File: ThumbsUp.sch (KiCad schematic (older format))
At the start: 150 parts, among them IC1 RP2040, IC2 W25Q128JVSIM, J1 Conn_01x04_Male, J10 Raiser_Male, J11 Raiser_Female, J12 Raiser_Male, J13 Raiser_Female, J14 Raiser_Male, J15 Raiser_Female, J16 Raiser_Male, J17 Raiser_Female, J18 Raiser_Male, J19 52559-1233, J2 Conn_01x04_Male, J20 Conn_01x04_Female, J21 Conn_01x04_Female, J22 Conn_01x04_Female, J23 Conn_01x04_Female, J24 Conn_01x04_Male, J25 Conn_01x04_Male, J26 Conn_01x04_Male, J27 Conn_01x04_Male, J28 Conn_01x04_Female, J29 Conn_01x04_Female, J3 Conn_01x04_Female, J30 Conn_01x04_Female, J31 Conn_01x04_Female, J4 Conn_01x04_Male, J5 Conn_01x04_Female, J6 Conn_01x04_Male, J7 Conn_01x04_Male, J8 Conn_01x04_Male, J9 Raiser_Female, U1 NCP1117-3.3_SOT223, Y1 ABLS-12.000MHZ-B4-T

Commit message: Wiring continued
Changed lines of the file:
@@
 Wire Wire Line
 	12550 2900 12200 2900
-$Comp
-L RP2040:RP2040 IC1
-U 1 1 6393717F
-P 2050 2550
-F 0 "IC1" H 4094 1996 50  0000 L CNN
-F 1 "RP2040" H 4094 1905 50  0000 L CNN
-F 2 "RP2040:QFN40P700X700X90-57N-D" H 3900 3250 50  0001 L CNN
-F 3 "https://datasheets.raspberrypi.org/rp2040/rp2040-datasheet.pdf" H 3900 3150 50  0001 L CNN
-F 4 "Microcontroller in QFN Package" H 3900 3050 50  0001 L CNN "Description"
-F 5 "0.9" H 3900 2950 50  0001 L CNN "Height"
-F 6 "RASPBERRY-PI" H 3900 2850 50  0001 L CNN "Manufacturer_Name"
-F 7 "RP2040" H 3900 2750 50  0001 L CNN "Manufacturer_Part_Number"
-F 8 "" H 3900 2650 50  0001 L CNN "Mouser Part Number"
-F 9 "" H 3900 2550 50  0001 L CNN "Mouser Price/Stock"
-F 10 "" H 3900 2450 50  0001 L CNN "Arrow Part Number"
-F 11 "" H 3900 2350 50  0001 L CNN "Arrow Price/Stock"
-F 12 "" H 3900 2250 50  0001 L CNN "Mouser Testing Part Number"
-F 13 "" H 3900 2150 50  0001 L CNN "Mouser Testing Price/Stock"
-	1    2050 2550
-	1    0    0    -1
-$EndComp
 Wire Wire Line
 	2050 3450 1550 3450
@@
 Wire Wire Line
 	3050 5100 1550 5100
-Wire Wire Line
-	1550 5100 1550 3450
 Connection ~ 1550 3450
 Wire Wire Line
@@
 Wire Wire Line
 	1550 1200 1550 2550
-Wire Wire Line
-	2050 2550 1550 2550
 Connection ~ 1550 2550
 Wire Wire Line
@@
 	3550 5050 3550 5350
 Connection ~ 3550 5350
+Wire Wire Line
+	1550 5100 1550 3450
+Wire Wire Line
+	2050 2550 1550 2550
+$Comp
+L RP2040:RP2040 IC1
+U 1 1 6393717F
+P 2050 2550
+F 0 "IC1" H 4094 1996 50  0000 L CNN
+F 1 "RP2040" H 4094 1905 50  0000 L CNN
+F 2 "RP2040:QFN40P700X700X90-57N-D" H 3900 3250 50  0001 L CNN
+F 3 "https://datasheets.raspberrypi.org/rp2040/rp2040-datasheet.pdf" H 3900 3150 50  0001 L CNN
+F 4 "Microcontroller in QFN Package" H 3900 3050 50  0001 L CNN "Description"
+F 5 "0.9" H 3900 2950 50  0001 L CNN "Height"
+F 6 "RASPBERRY-PI" H 3900 2850 50  0001 L CNN "Manufacturer_Name"
+F 7 "RP2040" H 3900 2750 50  0001 L CNN "Manufacturer_Part_Number"
+F 8 "" H 3900 2650 50  0001 L CNN "Mouser Part Number"
+F 9 "" H 3900 2550 50  0001 L CNN "Mouser Price/Stock"
+F 10 "" H 3900 2450 50  0001 L CNN "Arrow Part Number"
+F 11 "" H 3900 2350 50  0001 L CNN "Arrow Price/Stock"
+F 12 "" H 3900 2250 50  0001 L CNN "Mouser Testing Part Number"
+F 13 "" H 3900 2150 50  0001 L CNN "Mouser Testing Price/Stock"
+	1    2050 2550
+	1    0    0    -1
+$EndComp
+Text GLabel 4050 2650 2    50   Input ~ 0
+ROW2
+Text GLabel 4050 2750 2    50   Input ~ 0
+ROW3
+Text GLabel 4050 2850 2    50   Input ~ 0
+COL5
+Text GLabel 4050 2950 2    50   Input ~ 0
+COL3
+Text GLabel 4050 3050 2    50   Input ~ 0
+COL2
+Text GLabel 4050 3150 2    50   Input ~ 0
+COL1
+Text GLabel 4050 3250 2    50   Input ~ 0
+COL0
+Text GLabel 4050 3350 2    50   Input ~ 0
+COL4
+Text GLabel 2050 2650 0    50   Input ~ 0
+ROW0
+Text GLabel 2050 2750 0    50   Input ~ 0
+ROW1
+Text GLabel 2050 2850 0    50   Input ~ 0
+COL7
+Text GLabel 2050 2950 0    50   Input ~ 0
+COL6
+Text GLabel 2050 3050 0    50   Input ~ 0
+COL8
+Text GLabel 2050 3150 0    50   Input ~ 0
+COL9
+Text GLabel 2050 3250 0    50   Input ~ 0
+COLA
+Text GLabel 2050 3350 0    50   Input ~ 0
+COLB
 $EndSCHEMATC

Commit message: Replaced the mini-USB connector with USB-C
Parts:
- removed USB1: Molex-0548190589, random-keyboard-parts:Molex-0548190589, symbol ThumbsUp-rescue:Molex-0548190589-random-keyboard-parts
- added J32: USB_C_Receptacle_USB2.0, Connector_USB:USB_C_Receptacle_Palconn_UTC16-G, symbol Connector:USB_C_Receptacle_USB2.0
- added R8, R9: 5.1k, Resistor_SMD:R_0805_2012Metric, symbol Device:R_Small
- BOOTSEL1, RUN1: footprint TL1016AAF220QG -> TL1016AAF220QG:TL1016AAF220QG
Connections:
- wire segments 474 -> 481
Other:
- moved on the sheet: BOOTSEL1, C1, C10, C12, C13, C14, C15, C16, C17, C2, C3, C4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

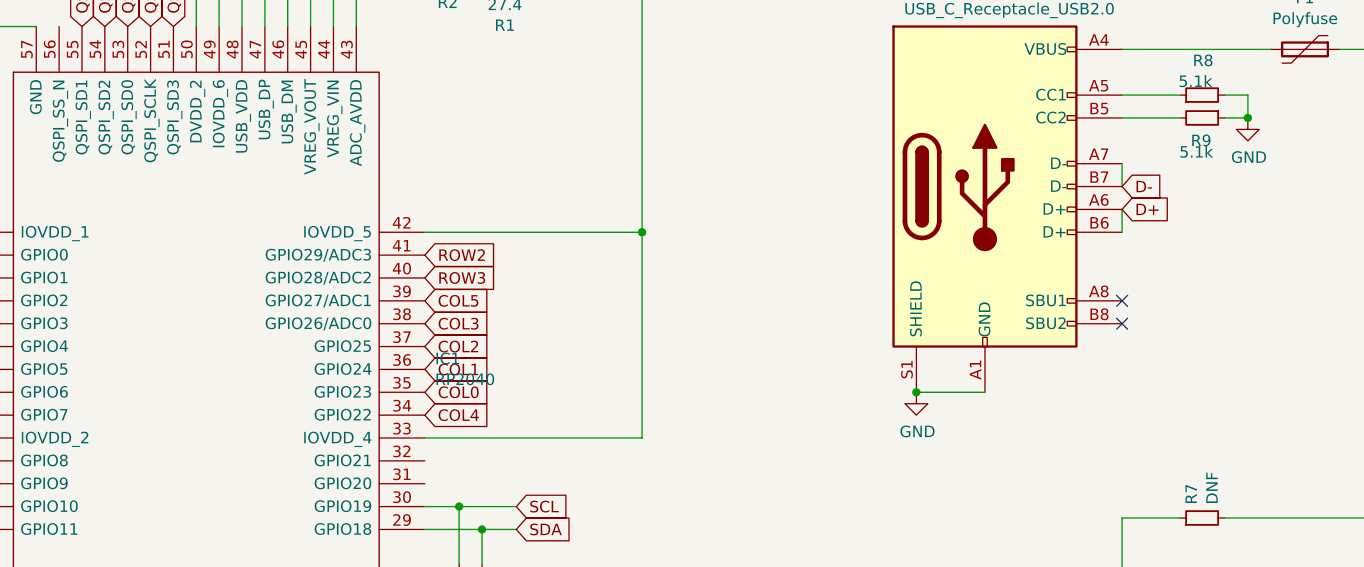
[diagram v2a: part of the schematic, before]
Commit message: Some schema elements rearranged
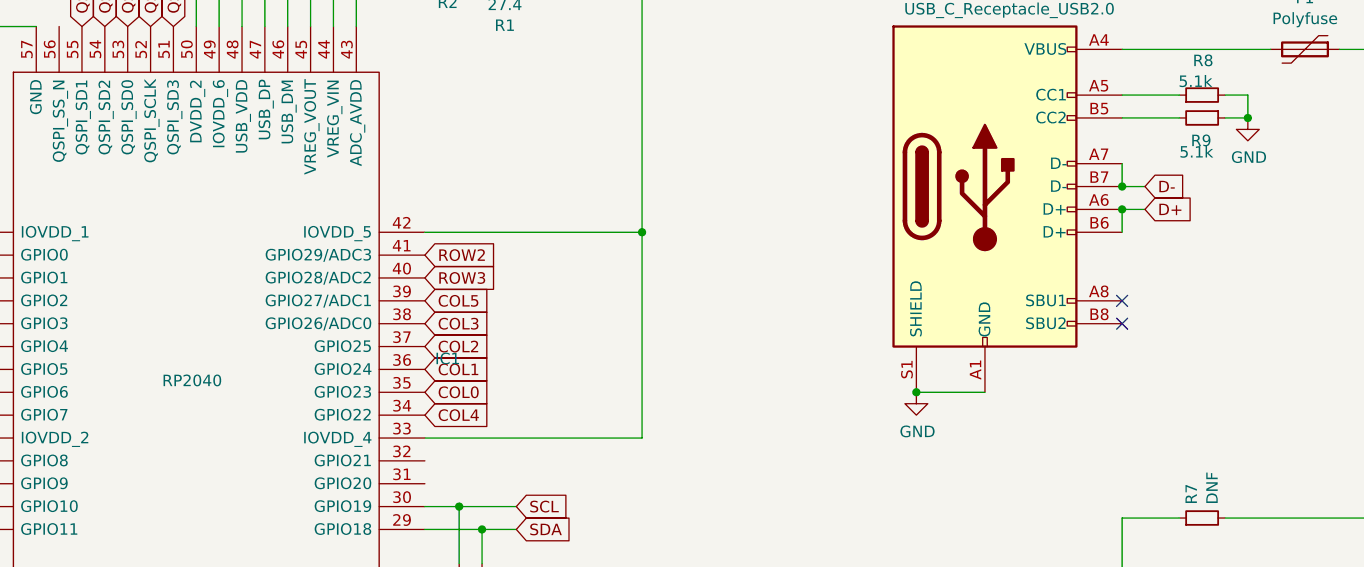
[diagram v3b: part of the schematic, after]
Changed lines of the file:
@@
 Wire Wire Line
 	8350 1600 8350 1750
-Text GLabel 7100 2350 2    50   Input ~ 0
+Text GLabel 7200 2350 2    50   Input ~ 0
 D-
-Text GLabel 7100 2450 2    50   Input ~ 0
+Text GLabel 7200 2450 2    50   Input ~ 0
 D+
 $Comp
@@
 P 2050 2550
 F 0 "IC1" H 4094 1996 50  0000 L CNN
-F 1 "RP2040" H 4094 1905 50  0000 L CNN
+F 1 "RP2040" H 2900 1900 50  0000 L CNN
 F 2 "RP2040:QFN40P700X700X90-57N-D" H 3900 3250 50  0001 L CNN
 F 3 "https://datasheets.raspberrypi.org/rp2040/rp2040-datasheet.pdf" H 3900 3150 50  0001 L CNN
@@
 NoConn ~ 7100 2850
 NoConn ~ 7100 2950
+Wire Wire Line
+	7100 2350 7200 2350
+Connection ~ 7100 2350
+Wire Wire Line
+	7100 2450 7200 2450
+Connection ~ 7100 2450
 $EndSCHEMATC

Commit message: Restored the schematics file which was overridden by mistake
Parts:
- added J33: STX-3501-3N, STX-3501-3N:STX35013N, symbol STX-3501-3N:STX-3501-3N
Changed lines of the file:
@@
 	7100 2450 7200 2450
 Connection ~ 7100 2450
+$Comp
+L STX-3501-3N:STX-3501-3N J33
+U 1 1 63B2DFF1
+P 8200 2800
+F 0 "J33" H 8600 3065 50  0000 C CNN
+F 1 "STX-3501-3N" H 8600 2974 50  0000 C CNN
+F 2 "STX-3501-3N:STX35013N" H 8850 2900 50  0001 L CNN
+F 3 "https://datasheet.datasheetarchive.com/originals/distributors/Datasheets_SAMA/ae9d1df0991347f2f81145ba35ca04dc.pdf" H 8850 2800 50  0001 L CNN
+F 4 "Phone Connectors 3.5mm S LUGS STEREO 3P THRU HOLE" H 8850 2700 50  0001 L CNN "Description"
+F 5 "5" H 8850 2600 50  0001 L CNN "Height"
+F 6 "Kycon" H 8850 2500 50  0001 L CNN "Manufacturer_Name"
+F 7 "STX-3501-3N" H 8850 2400 50  0001 L CNN "Manufacturer_Part_Number"
+F 8 "806-STX-3501-3N" H 8850 2300 50  0001 L CNN "Mouser Part Number"
+F 9 "https://www.mouser.co.uk/ProductDetail/Kycon/STX-3501-3N?qs=BBNwCsfFaznpJt4o1Jp%2FTg%3D%3D" H 8850 2200 50  0001 L CNN "Mouser Price/Stock"
+F 10 "" H 8850 2100 50  0001 L CNN "Arrow Part Number"
+F 11 "" H 8850 2000 50  0001 L CNN "Arrow Price/Stock"
+F 12 "" H 8850 1900 50  0001 L CNN "Mouser Testing Part Number"
+F 13 "" H 8850 1800 50  0001 L CNN "Mouser Testing Price/Stock"
+	1    8200 2800
+	1    0    0    -1
+$EndComp
 $EndSCHEMATC

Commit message: Added a missing line SS-N
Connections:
- net labels added: QSPI_SSN
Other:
- moved on the sheet: BOOTSEL1, R3
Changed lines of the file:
@@
 L Device:R_Small R3
 U 1 1 616D4E45
-P 7000 4350
-F 0 "R3" H 7059 4396 50  0000 L CNN
-F 1 "10k" H 7059 4305 50  0000 L CNN
-F 2 "Resistor_SMD:R_0805_2012Metric" H 7000 4350 50  0001 C CNN
-F 3 "~" H 7000 4350 50  0001 C CNN
-	1    7000 4350
+P 7000 3800
+F 0 "R3" H 7059 3846 50  0000 L CNN
+F 1 "10k" H 7059 3755 50  0000 L CNN
+F 2 "Resistor_SMD:R_0805_2012Metric" H 7000 3800 50  0001 C CNN
+F 3 "~" H 7000 3800 50  0001 C CNN
+	1    7000 3800
 	0    -1   -1   0
 $EndComp
@@
 	3350 1350 3350 1650
 $Comp
-L W25Q128JVSIM:W25Q128JVSIM IC2
-U 1 1 64048C65
-P 7100 4350
-F 0 "IC2" H 8200 4615 50  0000 C CNN
-F 1 "W25Q128JVSIM" H 8200 4524 50  0000 C CNN
-F 2 "W25Q128JVSIM:SOIC127P790X216-8N" H 9150 4450 50  0001 L CNN
-F 3 "https://www.winbond.com/hq/search-resource-file.jsp?partNo=W25Q128JVSIM&type=datasheet" H 9150 4350 50  0001 L CNN
-F 4 "128M-bit Serial Flash Memory with uniform 4KB sectors and Dual/Quad SPI" H 9150 4250 50  0001 L CNN "Description"
-F 5 "2.16" H 9150 4150 50  0001 L CNN "Height"
-F 6 "Winbond" H 9150 4050 50  0001 L CNN "Manufacturer_Name"
-F 7 "W25Q128JVSIM" H 9150 3950 50  0001 L CNN "Manufacturer_Part_Number"
-F 8 "454-W25Q128JVSIM" H 9150 3850 50  0001 L CNN "Mouser Part Number"
-F 9 "https://www.mouser.co.uk/ProductDetail/Winbond/W25Q128JVSIM?qs=qSfuJ%252Bfl%2Fd6d7A5WLggp6w%3D%3D" H 9150 3750 50  0001 L CNN "Mouser Price/Stock"
-F 10 "W25Q128JVSIM" H 9150 3650 50  0001 L CNN "Arrow Part Number"
-F 11 "https://www.arrow.com/en/products/w25q128jvsim/winbond-electronics?region=nac" H 9150 3550 50  0001 L CNN "Arrow Price/Stock"
-F 12 "" H 9150 3450 50  0001 L CNN "Mouser Testing Part Number"
-F 13 "" H 9150 3350 50  0001 L CNN "Mouser Testing Price/Stock"
-	1    7100 4350
-	1    0    0    -1
-$EndComp
-$Comp
 L Device:C_Small C10
 U 1 1 6404A526
@@
 L TL1016AAF220QG:TL1016AAF220QG BOOTSEL1
 U 1 1 63B7CD0C
-P 6250 4350
-F 0 "BOOTSEL1" V 6100 4100 50  0000 L CNN
-F 1 "TL1016AAF220QG" V 6200 4000 50  0000 L CNN
-F 2 "TL1016AAF220QG:TL1016AAF220QG" H 6900 4450 50  0001 L CNN
-F 3 "https://eu.mouser.com/datasheet/2/140/E_Switch_05112022_TL1016_Datasheet-2943618.pdf" H 6900 4350 50  0001 L CNN
-F 4 "Tactile Switches Tactile Switch SPST OFF-(ON) 50mA 12VDC" H 6900 4250 50  0001 L CNN "Description"
-F 5 "1.35" H 6900 4150 50  0001 L CNN "Height"
-F 6 "E-Switch" H 6900 4050 50  0001 L CNN "Manufacturer_Name"
-F 7 "TL1016AAF220QG" H 6900 3950 50  0001 L CNN "Manufacturer_Part_Number"
-F 8 "612-TL1016AAF220QG" H 6900 3850 50  0001 L CNN "Mouser Part Number"
-F 9 "https://www.mouser.co.uk/ProductDetail/E-Switch/TL1016AAF220QG?qs=t7xnP681wgW5zrSpkWH91Q%3D%3D" H 6900 3750 50  0001 L CNN "Mouser Price/Stock"
-F 10 "" H 6900 3650 50  0001 L CNN "Arrow Part Number"
-F 11 "" H 6900 3550 50  0001 L CNN "Arrow Price/Stock"
-F 12 "" H 6900 3450 50  0001 L CNN "Mouser Testing Part Number"
-F 13 "" H 6900 3350 50  0001 L CNN "Mouser Testing Price/Stock"
-	1    6250 4350
+P 6250 3800
+F 0 "BOOTSEL1" V 6100 3550 50  0000 L CNN
+F 1 "TL1016AAF220QG" V 6200 3450 50  0000 L CNN
+F 2 "TL1016AAF220QG:TL1016AAF220QG" H 6900 3900 50  0001 L CNN
+F 3 "https://eu.mouser.com/datasheet/2/140/E_Switch_05112022_TL1016_Datasheet-2943618.pdf" H 6900 3800 50  0001 L CNN
+F 4 "Tactile Switches Tactile Switch SPST OFF-(ON) 50mA 12VDC" H 6900 3700 50  0001 L CNN "Description"
+F 5 "1.35" H 6900 3600 50  0001 L CNN "Height"
+F 6 "E-Switch" H 6900 3500 50  0001 L CNN "Manufacturer_Name"
+F 7 "TL1016AAF220QG" H 6900 3400 50  0001 L CNN "Manufacturer_Part_Number"
+F 8 "612-TL1016AAF220QG" H 6900 3300 50  0001 L CNN "Mouser Part Number"
+F 9 "https://www.mouser.co.uk/ProductDetail/E-Switch/TL1016AAF220QG?qs=t7xnP681wgW5zrSpkWH91Q%3D%3D" H 6900 3200 50  0001 L CNN "Mouser Price/Stock"
+F 10 "" H 6900 3100 50  0001 L CNN "Arrow Part Number"
+F 11 "" H 6900 3000 50  0001 L CNN "Arrow Price/Stock"
+F 12 "" H 6900 2900 50  0001 L CNN "Mouser Testing Part Number"
+F 13 "" H 6900 2800 50  0001 L CNN "Mouser Testing Price/Stock"
+	1    6250 3800
 	0    1    1    0
 $EndComp
 Wire Wire Line
-	6250 4350 6450 4350
-Wire Wire Line
-	6250 5150 6450 5150
+	6250 3800 6450 3800
 Wire Wire Line
-	6450 5150 6450 4350
-Connection ~ 6450 4350
+	6250 4600 6450 4600
 Wire Wire Line
-	6450 4350 6900 4350
+	6450 4600 6450 3800
+Connection ~ 6450 3800
 Wire Wire Line
-	6150 4350 5950 4350
+	6150 3800 5950 3800
 Wire Wire Line
-	5950 4350 5950 5150
+	5950 3800 5950 4600
 Wire Wire Line
-	5950 5150 6150 5150
+	5950 4600 6150 4600
 $Comp
 L power:GND #PWR0120
 U 1 1 63D2EFAD
-P 5950 5150
-F 0 "#PWR0120" H 5950 4900 50  0001 C CNN
-F 1 "GND" H 5955 4977 50  0000 C CNN
-F 2 "" H 5950 5150 50  0001 C CNN
-F 3 "" H 5950 5150 50  0001 C CNN
-	1    5950 5150
+P 5950 4600
+F 0 "#PWR0120" H 5950 4350 50  0001 C CNN
+F 1 "GND" H 5955 4427 50  0000 C CNN
+F 2 "" H 5950 4600 50  0001 C CNN
+F 3 "" H 5950 4600 50  0001 C CNN
+	1    5950 4600
 	1    0    0    -1
 $EndComp
-Connection ~ 5950 5150
+Connection ~ 5950 4600
 Wire Wire Line
 	1550 1200 1550 2550
@@
 	1    0    0    -1
 $EndComp
+Text GLabel 2450 1650 1    50   Input ~ 0
+QSPI_SSN
+Text GLabel 7100 4350 0    50   Input ~ 0
+QSPI_SSN
+Wire Wire Line
+	6450 3800 6900 3800
+$Comp
+L W25Q128JVSIM:W25Q128JVSIM IC2
+U 1 1 64048C65
+P 7100 4350
+F 0 "IC2" H 8200 4615 50  0000 C CNN
+F 1 "W25Q128JVSIM" H 8200 4524 50  0000 C CNN
+F 2 "W25Q128JVSIM:SOIC127P790X216-8N" H 9150 4450 50  0001 L CNN
+F 3 "https://www.winbond.com/hq/search-resource-file.jsp?partNo=W25Q128JVSIM&type=datasheet" H 9150 4350 50  0001 L CNN
+F 4 "128M-bit Serial Flash Memory with uniform 4KB sectors and Dual/Quad SPI" H 9150 4250 50  0001 L CNN "Description"
+F 5 "2.16" H 9150 4150 50  0001 L CNN "Height"
+F 6 "Winbond" H 9150 4050 50  0001 L CNN "Manufacturer_Name"
+F 7 "W25Q128JVSIM" H 9150 3950 50  0001 L CNN "Manufacturer_Part_Number"
+F 8 "454-W25Q128JVSIM" H 9150 3850 50  0001 L CNN "Mouser Part Number"
+F 9 "https://www.mouser.co.uk/ProductDetail/Winbond/W25Q128JVSIM?qs=qSfuJ%252Bfl%2Fd6d7A5WLggp6w%3D%3D" H 9150 3750 50  0001 L CNN "Mouser Price/Stock"
+F 10 "W25Q128JVSIM" H 9150 3650 50  0001 L CNN "Arrow Part Number"
+F 11 "https://www.arrow.com/en/products/w25q128jvsim/winbond-electronics?region=nac" H 9150 3550 50  0001 L CNN "Arrow Price/Stock"
+F 12 "" H 9150 3450 50  0001 L CNN "Mouser Testing Part Number"
+F 13 "" H 9150 3350 50  0001 L CNN "Mouser Testing Price/Stock"
+	1    7100 4350
+	1    0    0    -1
+$EndComp
+Connection ~ 7100 3800
 $EndSCHEMATC
